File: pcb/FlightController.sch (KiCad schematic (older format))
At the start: 28 parts, among them P2 USB_OTG, P3 CONN_02X04, P4 CKD_SANDWICH, U1 MPU-6500, U2 STM32F303x{B,C}, Y1 8Mhz

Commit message: v2 of the f3fc which adds pull up resistors for the i2c lines.
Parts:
- added RP1: R_PACK4, Resistors_SMD:R_Array_Convex_4x1206, symbol R_PACK4
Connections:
- wire segments 187 -> 189
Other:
- moved on the sheet: R7, R8

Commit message: v3 of f3fc. Correct mosfet pinout. Add measurement points. Remove MPU. Tweaked pinout with one less SPI.
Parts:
- removed C1: 0.01uf, Capacitors_SMD:C_0603_HandSoldering, symbol C_Small
- removed C4, C6: 0.1uF, Capacitors_SMD:C_0603_HandSoldering, symbol C_Small
- removed RP1: R_PACK4, Resistors_SMD:R_Array_Convex_4x1206, symbol R_PACK4
- removed U1: MPU-6500, Housings_DFN_QFN:QFN-24-1EP_3x3mm_Pitch0.4mm, symbol MPU-6500
- added P10: SWDIO, Measurement_Points:Measurement_Point_Round-SMD-Pad_Small, symbol CONN_01X01
- added P11: SWCLK, Measurement_Points:Measurement_Point_Round-SMD-Pad_Small, symbol CONN_01X01
- added R11, R4: 4.7k, Resistors_SMD:R_0603_HandSoldering, symbol R_Small
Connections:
- net labels added: GPIO1_5, GPIO2_4, GPIO3_3, GPIO4_2, PB7, SWDIO_13, TIM8_CH2_SWCLK
- net labels removed: GPIO1, GPIO2, GPIO3, GPIO4, MPU_INT, SPI1_MISO, SPI1_MOSI, SPI1_NSS, SPI1_SCK, TIM8_CH2, xi2c_SCL, xi2c_SDA
- wire segments 189 -> 171
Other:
- note added: "Chickadee Tech F3FC v3"
- note removed: "Chickadee Tech F3FC v1"

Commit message: Move decoupling caps to the front side of the board, re-add the MPU and switch from a crystal to a resonator.
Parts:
- removed Y1: 8Mhz, abracon:ABM7, symbol Crystal
- added C1: 10000pF, Capacitors_SMD:C_0603_HandSoldering, symbol C_Small
- added U1: MPU-6500, invensense:QFN-24-1EP_3x3mm_Pitch0.4mm, symbol MPU-6500
- added X1: 8MHZ, murata-resonator:CSTCE_G-CSTCE_G_Z, symbol CRYSTAL_SMD
- C10, C7, C8, C9: value 100nF -> 0.1uF
- C2, C3: value 27pF -> 0.1uF; footprint Capacitors_SMD:C_0402 -> Capacitors_SMD:C_0603_HandSoldering
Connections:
- net labels added: MPU_INT, SPI1_MISO, SPI1_MOSI, SPI1_NSS, SPI1_SCK
- wire segments 171 -> 184
- no-connect marks 48 -> 45
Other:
- note added: "Chickadee Tech F3FC v4"
- note removed: "Chickadee Tech F3FC v3"

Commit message: v5 of F3FC. Adjusts motor output location, switches to MPU-6000 and adds chickadee logo back.
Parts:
- removed R7: 100k, Resistors_SMD:R_0603_HandSoldering, symbol R
- removed R8: 10k, Resistors_SMD:R_0603_HandSoldering, symbol R
- removed U1: MPU-6500, invensense:QFN-24-1EP_3x3mm_Pitch0.4mm, symbol MPU-6500
- added U1: MPU-6000, Housings_DFN_QFN:QFN-24-1EP_4x4mm_Pitch0.5mm, symbol MPU-6000
- C1: value 10000pF -> 2.2nF
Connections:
- net labels added: PA14_SWCLK
- net labels removed: BATT_ADC, GPIO1_5, TIM8_CH2_SWCLK
- wire segments 184 -> 175
- no-connect marks 45 -> 50

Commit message: F3FC v6 which features correct reset circuitry.
Also:
* Routes USB as differential pair.
* Corrects reset circuit.
* Adds fiducials
* Matches up LED numbering to reference
* Supports current pin from power connector.
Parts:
- D1: renamed from D3; value LED -> Green
- D2: value LED -> Yellow
- D3: renamed from D1; value LED -> Red
- renumbered R3 to R1, R1 to R3
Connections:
- net labels added: CURRENT, USB_D+, USB_D-
- net labels removed: USB_DM, USB_DP
- no-connect marks 50 -> 49
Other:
- note added: "Chickadee Tech F3FC v6"
- note removed: "Chickadee Tech F3FC v4"
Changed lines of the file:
@@
 si2c_SDA
 Text Label 6450 3000 0    60   ~ 0
-USB_DM
+USB_D-
 Text Label 6450 2900 0    60   ~ 0
-USB_DP
+USB_D+
 $Comp
 L GNDPWR #PWR03
@@
 $EndComp
 Text Label 4450 6450 0    60   ~ 0
-USB_DP
+USB_D+
 Text Label 4550 6600 0    60   ~ 0
-USB_DM
+USB_D-
 $Comp
 L +5V #PWR07
@@
 Text Label 2150 2700 2    60   ~ 0
 GPIO2_4
-NoConn ~ 2150 4200
 NoConn ~ 2150 4300
 NoConn ~ 2150 4700
@@
 LED2
 $Comp
-L LED D1
+L LED D3
 U 1 1 563331FB
 P 900 1050
-F 0 "D1" H 900 1150 50  0000 C CNN
-F 1 "LED" H 900 950 50  0000 C CNN
+F 0 "D3" H 900 1150 50  0000 C CNN
+F 1 "Red" H 900 950 50  0000 C CNN
 F 2 "LEDs:LED-0603" H 900 1050 60  0001 C CNN
 F 3 "" H 900 1050 60  0000 C CNN
@@
 P 900 1350
 F 0 "D2" H 900 1450 50  0000 C CNN
-F 1 "LED" H 900 1250 50  0000 C CNN
+F 1 "Yellow" H 900 1250 50  0000 C CNN
 F 2 "LEDs:LED-0603" H 900 1350 60  0001 C CNN
 F 3 "" H 900 1350 60  0000 C CNN
@@
 $EndComp
 $Comp
-L LED D3
+L LED D1
 U 1 1 56333271
 P 900 1650
-F 0 "D3" H 900 1750 50  0000 C CNN
-F 1 "LED" H 900 1550 50  0000 C CNN
+F 0 "D1" H 900 1750 50  0000 C CNN
+F 1 "Green" H 900 1550 50  0000 C CNN
 F 2 "LEDs:LED-0603" H 900 1650 60  0001 C CNN
 F 3 "" H 900 1650 60  0000 C CNN
@@
 $EndComp
 $Comp
-L R_Small R1
+L R_Small R3
 U 1 1 563338B7
 P 1300 1050
-F 0 "R1" H 1330 1070 50  0000 L CNN
+F 0 "R3" H 1330 1070 50  0000 L CNN
 F 1 "1k" H 1330 1010 50  0000 L CNN
 F 2 "Resistors_SMD:R_0603_HandSoldering" H 1300 1050 60  0001 C CNN
@@
 $EndComp
 $Comp
-L R_Small R3
+L R_Small R1
 U 1 1 56333942
 P 1300 1650
-F 0 "R3" H 1330 1670 50  0000 L CNN
+F 0 "R1" H 1330 1670 50  0000 L CNN
 F 1 "1k" H 1330 1610 50  0000 L CNN
 F 2 "Resistors_SMD:R_0603_HandSoldering" H 1300 1650 60  0001 C CNN
@@
 F0 "Power" 60
 F1 "Power.sch" 60
+F2 "CURRENT" I R 7800 5900 60
 $EndSheet
 Text Notes 9350 6900 2    118  ~ 0
-Chickadee Tech F3FC v4
+Chickadee Tech F3FC v6
 $Comp
 L VDD #PWR018
@@
 Text Label 5400 1450 1    60   ~ 0
 PA14_SWCLK
+Text Label 7800 5900 0    60   ~ 0
+CURRENT
+Text Label 2150 4200 2    60   ~ 0
+CURRENT
 $EndSCHEMATC

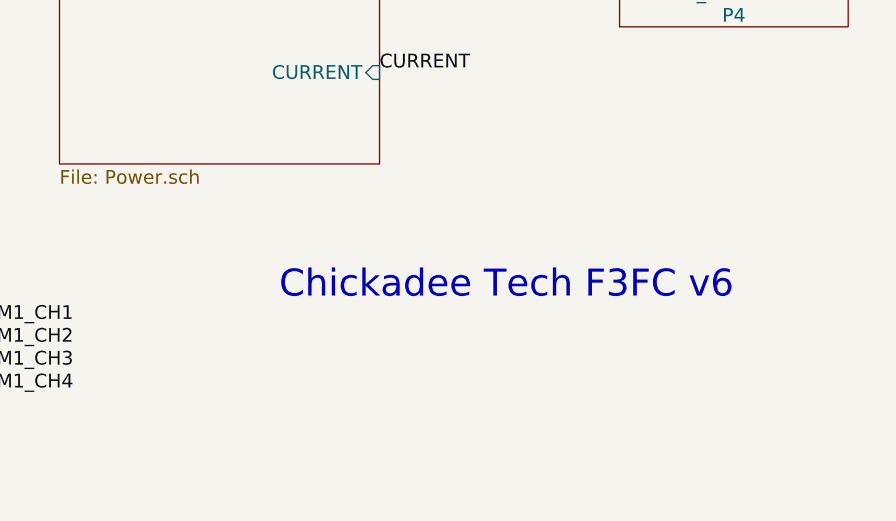
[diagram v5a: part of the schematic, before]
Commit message: Update polystack logo to bold variant and bump version number.
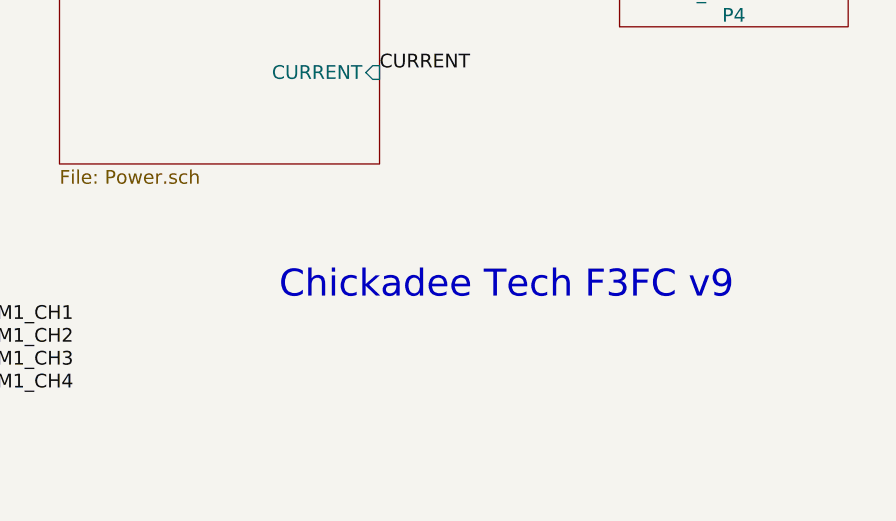
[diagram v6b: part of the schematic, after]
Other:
- note added: "Chickadee Tech F3FC v9"
- note removed: "Chickadee Tech F3FC v6"
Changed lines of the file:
@@
 $EndSheet
 Text Notes 9350 6900 2    118  ~ 0
-Chickadee Tech F3FC v6
+Chickadee Tech F3FC v9
 $Comp
 L VDD #PWR018

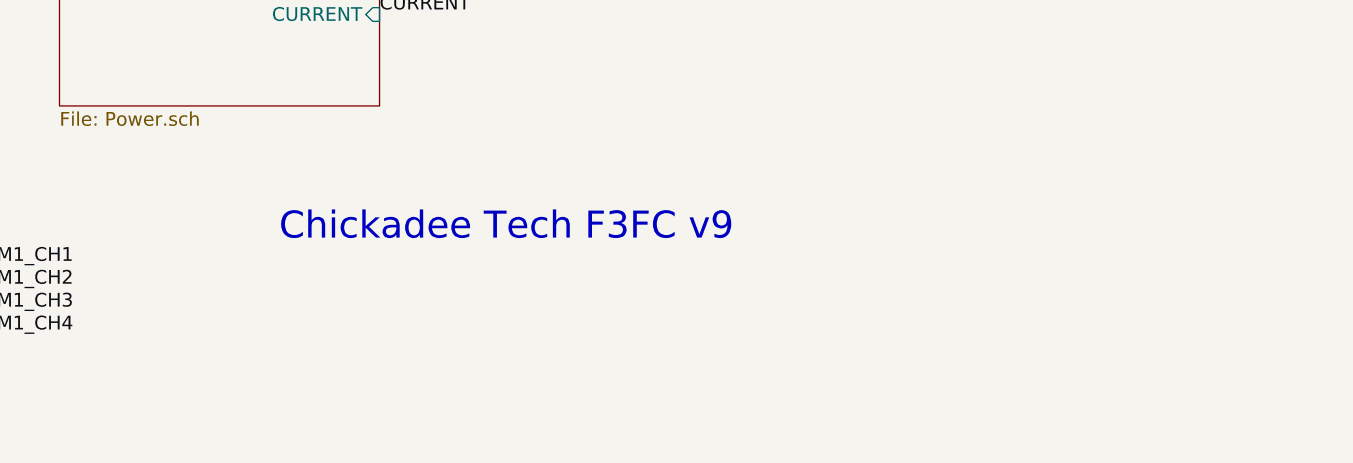
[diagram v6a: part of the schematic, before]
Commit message: Add license information to many files. PCB design files are CC-BY and code is MIT license.
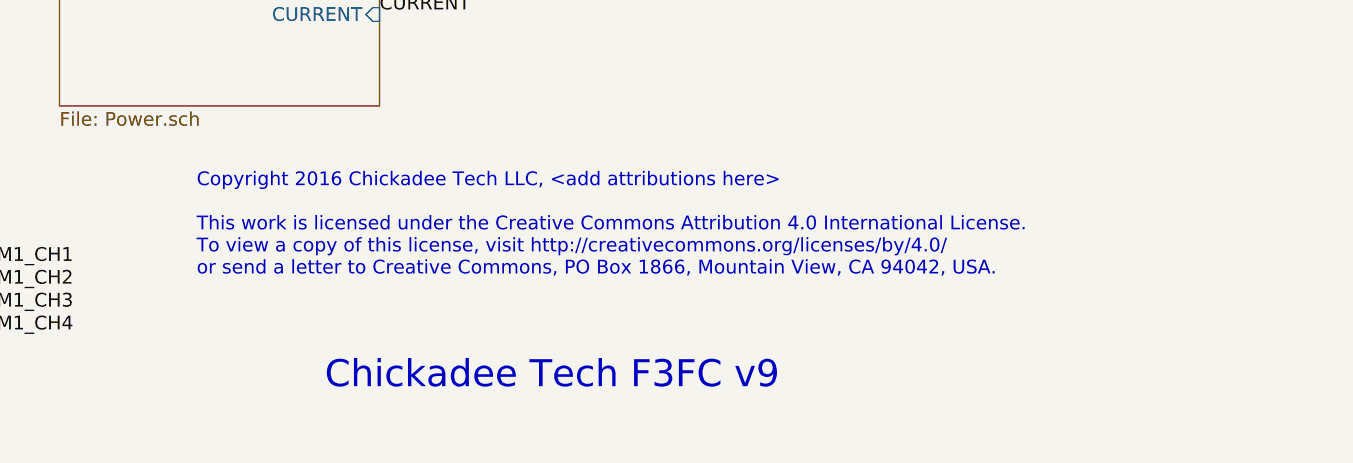
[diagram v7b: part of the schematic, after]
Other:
- note added: "Copyright 2016 Chickadee Tech LLC, <add attributions here>\n\nThis work is licensed under the Creative Commons Attribution 4.0 International License.\nTo view a copy of this license, visit http://creativecommons.org/licenses/by/4.0/\nor send a letter to Creative Commons, PO Box 1866, Mountain View, CA 94042, USA."
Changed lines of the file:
@@
 F2 "CURRENT" I R 7800 5900 60
 $EndSheet
-Text Notes 9350 6900 2    118  ~ 0
+Text Notes 9550 7550 2    118  ~ 0
 Chickadee Tech F3FC v9
 $Comp
@@
 Text Label 2150 4200 2    60   ~ 0
 CURRENT
+Text Notes 7000 7050 0    60   ~ 0
+Copyright 2016 Chickadee Tech LLC, <add attributions here>\n\nThis work is licensed under the Creative Commons Attribution 4.0 International License.\nTo view a copy of this license, visit http://creativecommons.org/licenses/by/4.0/\nor send a letter to Creative Commons, PO Box 1866, Mountain View, CA 94042, USA.
 $EndSCHEMATC

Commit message: Convert to relative component and footprint paths.
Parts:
- P4: value CKD_SANDWICH -> POLYSTACK_CONNECTOR; symbol CKD_SANDWICH -> POLYSTACK_CONNECTOR
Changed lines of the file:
@@
 LIBS:contrib
 LIBS:valves
-LIBS:ckd_sandwich
+LIBS:polystack
 LIBS:stm32
-LIBS:stm-ldo
-LIBS:ti-regu
-LIBS:ti-power-mux
 LIBS:invensense
-LIBS:FlightController-cache
 EELAYER 25 0
 EELAYER END
@@
 NoConn ~ 4900 1600
 $Comp
-L CKD_SANDWICH P4
+L POLYSTACK_CONNECTOR P4
 U 1 1 563C6361
 P 9350 1500
 F 0 "P4" H 9350 -2650 60  0000 C CNN
-F 1 "CKD_SANDWICH" H 9350 -2550 60  0000 C CNN
+F 1 "POLYSTACK_CONNECTOR" H 9350 -2550 60  0000 C CNN
 F 2 "hirose-df40:DF40-3-4mm-80pin-Receptacle" H 9350 -2700 60  0001 C CNN
 F 3 "" H 9350 -2700 60  0000 C CNN
